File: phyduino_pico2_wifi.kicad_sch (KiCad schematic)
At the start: 94 parts, among them J6 GT-USB-7047A, J9 GT-USB-7047A, Q1 SP30P25NQ, Q2 SP30P25NQ, U10 AP63200WU, U108 TPS2121RUXR, U109 TPS2121RUXR, U11 ESP32-C6-MINI-1-H4, U110 TPS2121RUXR, U6 AP33772SDKZ-13-FA02, U8 AP63200WU, U9 TPUSBLC6-2P6

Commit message: Built board without USB-PD variant. Not yet complete.
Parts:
- removed C132: 0.1µF, Capacitor_SMD [KL]:C_0402_1005Metric, symbol Device:C_Small
- removed C28: 0.1µF, Capacitor_SMD [KL]:C_1206_3216Metric_Pad1.33x1.80mm_HandSolder, symbol Component - Device [KL]:C_Small
- removed C29, C32: 10μF, Capacitor_SMD [KL]:C_0805_2012Metric_Pad1.18x1.45mm_HandSolder, symbol Component - Device [KL]:C_Small
- removed C30: 1µF, Capacitor_SMD [KL]:C_0402_1005Metric, symbol Component - Device [KL]:C_Small
- removed C31, C6: 0.1µF, Capacitor_SMD [KL]:C_0402_1005Metric, symbol Component - Device [KL]:C_Small
- removed C33, C35: 0.1μF, Capacitor_SMD [KL]:C_0805_2012Metric_Pad1.18x1.45mm_HandSolder, symbol Component - Device [KL]:C_Small
- removed J9: GT-USB-7047A, Connector - PC SMT [UL]:GCT-USBC-GCT_USB4110, symbol KL - Connector:USB_C_Receptacle_USB2.0_16P
- removed Q1, Q2: SP30P25NQ, Package_DFN_QFN [KL]:Diodes_UDFN2020-6_Type-F, symbol UL - Transistors - MOSFET:PMPB27EP
- removed R10: 5mΩ, Resistor_SMD [KL]:R_0603_1608Metric, symbol Component - Device [KL]:R_Small
- removed R11, R12, R7, R8: 5.1kΩ, Resistor_SMD [KL]:R_0402_1005Metric, symbol Component - Device [KL]:R_Small
- removed R143: 35.7kΩ, Resistor_SMD [KL]:R_0402_1005Metric, symbol Device:R_Small
- removed R149: 383kΩ, Resistor_SMD [KL]:R_0402_1005Metric, symbol Device:R_Small
- removed R150: 95.3kΩ, Resistor_SMD [KL]:R_0402_1005Metric, symbol Device:R_Small
- removed R151: 24.3kΩ, Resistor_SMD [KL]:R_0402_1005Metric, symbol Device:R_Small
- removed R37: 5.1kΩ, Resistor_SMD [KL]:R_0402_1005Metric, symbol phyduino_pico:R_Small
- removed R40, R41: 100Ω, Resistor_SMD [KL]:R_0402_1005Metric, symbol phyduino_pico:R_Small
- removed R9: 220kΩ, Resistor_SMD [KL]:R_0805_2012Metric_Pad1.20x1.40mm_HandSolder, symbol Component - Device [KL]:R_Small
- removed TH1: 10kΩ@25°C, Resistor_SMD [KL]:R_0402_1005Metric, symbol Component - Device [KL]:Thermistor_NTC
- removed TP10, TP11, TP13, TP18, TP2, TP4, TP5, TP6, TP7: TestPoint_Small, Component - Test point SMT [UL]:TestPoint_SameSky_CPG-47-TH-B, symbol Connector [KL]:TestPoint_Small
- removed U109: TPS2121RUXR, Package - QFN [UL]:VQFN-HR-12, symbol PMIC - TI:TPS2121RUX
- removed U6: AP33772SDKZ-13-FA02, Package_DFN_QFN [KL]:QFN-24-1EP_4x4mm_P0.5mm_EP2.75x2.75mm, symbol Interface - USB:AP33772S
- removed Z3: ESDA25P35-1U1M-ES, Diode_SMD [KL]:ST_QFN-2L_1.6x1.0mm, symbol phyduino_pico:D_Zener_Filled
- added TP27: TestPoint_Small, Component - Test point SMT [UL]:TestPoint_SameSky_CPG-47-TH-B, symbol Connector [KL]:TestPoint_Small
- C13, C131, C134: footprint Capacitor_SMD [KL]:C_0402_1005Metric -> Capacitor_SMD:C_0402_1005Metric
- C16, C24: value 0.1μF -> 0.1µF; footprint Capacitor_SMD [KL]:C_0805_2012Metric_Pad1.18x1.45mm_HandSolder -> Capacitor_SMD:C_0805_2012Metric_Pad1.18x1.45mm_HandSolder
- C17, C18, C25, C27, C36: footprint Capacitor_SMD [KL]:C_0805_2012Metric_Pad1.18x1.45mm_HandSolder -> Capacitor_SMD:C_0805_2012Metric_Pad1.18x1.45mm_HandSolder
- C19, C23, C37: value 10μF -> 10µF; footprint Capacitor_SMD [KL]:C_0805_2012Metric_Pad1.18x1.45mm_HandSolder -> Capacitor_SMD:C_0805_2012Metric_Pad1.18x1.45mm_HandSolder
- C5, C7: footprint Capacitor_SMD [KL]:C_0805_2012Metric_Pad1.18x1.45mm_HandSolder -> Capacitor_SMD:C_0402_1005Metric
- C9: footprint Capacitor_SMD [KL]:C_1206_3216Metric_Pad1.33x1.80mm_HandSolder -> Capacitor_SMD:C_1206_3216Metric_Pad1.33x1.80mm_HandSolder
- R134: value 42.2kΩ -> 42.2kΩ; footprint Resistor_SMD [KL]:R_0402_1005Metric -> Resistor_SMD:R_0402_1005Metric
- R135, R138: value 21kΩ -> 21kΩ; footprint Resistor_SMD [KL]:R_0402_1005Metric -> Resistor_SMD:R_0402_1005Metric
- R136, R137, R47, R48: value 5.1kΩ -> 5.1kΩ; footprint Resistor_SMD [KL]:R_0402_1005Metric -> Resistor_SMD:R_0402_1005Metric
- R140: value 113kΩ -> 113kΩ; footprint Resistor_SMD [KL]:R_0402_1005Metric -> Resistor_SMD:R_0402_1005Metric
- R141: value 432kΩ -> 432kΩ; footprint Resistor_SMD [KL]:R_0402_1005Metric -> Resistor_SMD:R_0402_1005Metric
- R142: value 52.3kΩ -> 52.3kΩ; footprint Resistor_SMD [KL]:R_0402_1005Metric -> Resistor_SMD:R_0402_1005Metric
- R144, R145: value 24.3kΩ -> 24.3kΩ; footprint Resistor_SMD [KL]:R_0402_1005Metric -> Resistor_SMD:R_0402_1005Metric
- R152: value 35.7kΩ -> 35.7kΩ; footprint Resistor_SMD [KL]:R_0402_1005Metric -> Resistor_SMD:R_0402_1005Metric
- R153: value 10kΩ -> 10kΩ; footprint Resistor_SMD [KL]:R_0402_1005Metric -> Resistor_SMD:R_0402_1005Metric
- R44, R45, R50, R55: footprint Resistor_SMD [KL]:R_0402_1005Metric -> Resistor_SMD:R_0402_1005Metric
- R51: value 47kΩ -> 47kΩ; footprint Resistor_SMD [KL]:R_0805_2012Metric_Pad1.20x1.40mm_HandSolder -> Resistor_SMD:R_0805_2012Metric_Pad1.20x1.40mm_HandSolder
- R52: value 16.5kΩ -> 16.5kΩ; footprint Resistor_SMD [KL]:R_0805_2012Metric_Pad1.20x1.40mm_HandSolder -> Resistor_SMD:R_0805_2012Metric_Pad1.20x1.40mm_HandSolder
- R56: value 196kΩ -> 196kΩ; footprint Resistor_SMD [KL]:R_0805_2012Metric_Pad1.20x1.40mm_HandSolder -> Resistor_SMD:R_0402_1005Metric
- R57: value 62kΩ -> 62kΩ; footprint Resistor_SMD [KL]:R_0805_2012Metric_Pad1.20x1.40mm_HandSolder -> Resistor_SMD:R_0402_1005Metric
- R58: value 157kΩ -> 157kΩ; footprint Resistor_SMD [KL]:R_0805_2012Metric_Pad1.20x1.40mm_HandSolder -> Resistor_SMD:R_0402_1005Metric
- R59: value 30kΩ -> 30kΩ; footprint Resistor_SMD [KL]:R_0805_2012Metric_Pad1.20x1.40mm_HandSolder -> Resistor_SMD:R_0402_1005Metric
- R6: footprint Resistor_SMD [KL]:R_0805_2012Metric_Pad1.20x1.40mm_HandSolder -> Resistor_SMD:R_0805_2012Metric_Pad1.20x1.40mm_HandSolder
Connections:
- net +VUSB_IN is gone; now on net +VIN: U110.7 (IN1)
- net DCDC_5V0_EN: now also TP27.1
- net GND: no longer U110.5 (OV1), U110.6 (PR1)
- net USB_COM_SHIELD: now also J6.S2 (SH); no longer J6.S1 (SH)
- net USB_PMUX1_CP2: now also U110.6 (PR1)
- net USB_PMUX1_OV2: now also U110.5 (OV1)
- no-connect marks 28 -> 17
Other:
- note removed: "5V to 20V"
- note removed: "9V to 20V"
- note removed: ">1.06V"
- note removed: "I^{2}C Addr = 0x52"
- note removed: "Overvoltage Protection = +22.0V"
- moved on the sheet: C131, C134, C16, C17, C18, C19, C23, C24, C25, C27, C36, C5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

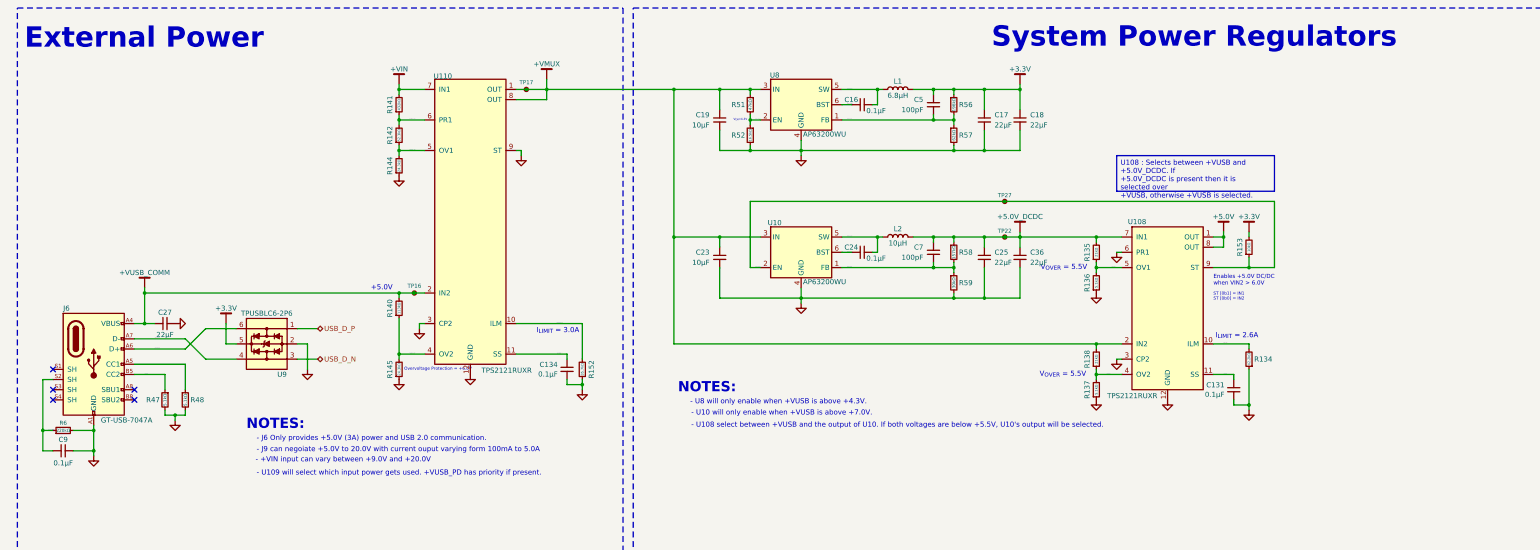
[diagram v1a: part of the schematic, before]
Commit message: Development update : Changed the power input and tree, removed led for communication status.
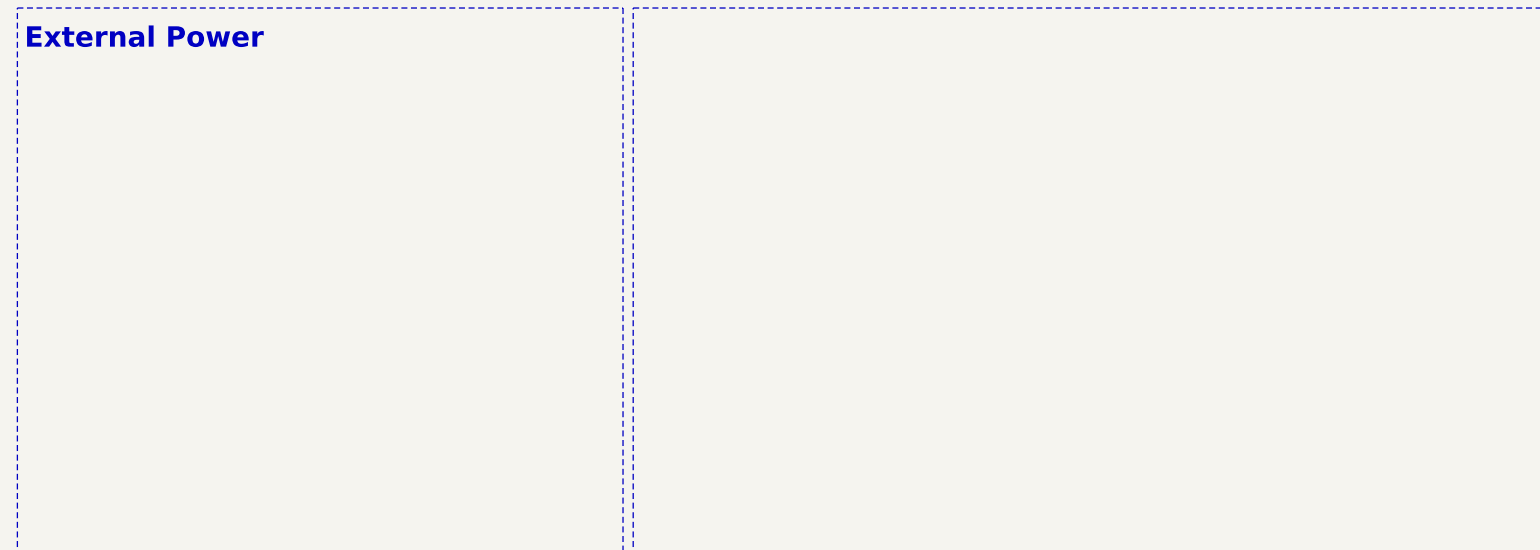
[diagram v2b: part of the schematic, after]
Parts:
- removed C131, C134: 0.1µF, Capacitor_SMD:C_0402_1005Metric, symbol Device:C_Small
- removed C16, C24: 0.1µF, Capacitor_SMD:C_0805_2012Metric_Pad1.18x1.45mm_HandSolder, symbol Component - Device [KL]:C_Small
- removed C17, C18, C25, C27, C36: 22µF, Capacitor_SMD:C_0805_2012Metric_Pad1.18x1.45mm_HandSolder, symbol Component - Device [KL]:C_Small
- removed C19, C23: 10µF, Capacitor_SMD:C_0805_2012Metric_Pad1.18x1.45mm_HandSolder, symbol Component - Device [KL]:C_Small
- removed C5, C7: 100pF, Capacitor_SMD:C_0402_1005Metric, symbol Component - Device [KL]:C_Small
- removed C9: 0.1µF, Capacitor_SMD:C_1206_3216Metric_Pad1.33x1.80mm_HandSolder, symbol Component - Device [KL]:C_Small
- removed J6: GT-USB-7047A, Connector - PC SMT [UL]:GCT-USBC-GCT_USB4110, symbol KL - Connector:USB_C_Receptacle_USB2.0_16P
- removed L1: 6.8µH, Component - Inductor SMT [UL]:L_Bourns_SRP4021HMCT, symbol Inductor - Bourns:L_Bourns_SRP4021HMCT-3R3M
- removed L2: 10µH, Component - Inductor SMT [UL]:L_Bourns_SRP4021HMCT, symbol Inductor - Bourns:L_Bourns_SRP4021HMCT-4R7M
- removed R134: 42.2kΩ, Resistor_SMD:R_0402_1005Metric, symbol Device:R_Small
- removed R135, R138: 21kΩ, Resistor_SMD:R_0402_1005Metric, symbol Device:R_Small
- removed R136, R137: 5.1kΩ, Resistor_SMD:R_0402_1005Metric, symbol Device:R_Small
- removed R140: 113kΩ, Resistor_SMD:R_0402_1005Metric, symbol Device:R_Small
- removed R141: 432kΩ, Resistor_SMD:R_0402_1005Metric, symbol Device:R_Small
- removed R142: 52.3kΩ, Resistor_SMD:R_0402_1005Metric, symbol Device:R_Small
- removed R144, R145: 24.3kΩ, Resistor_SMD:R_0402_1005Metric, symbol Device:R_Small
- removed R152: 35.7kΩ, Resistor_SMD:R_0402_1005Metric, symbol Device:R_Small
- removed R153: 10kΩ, Resistor_SMD:R_0402_1005Metric, symbol Device:R_Small
- removed R47, R48: 5.1kΩ, Resistor_SMD:R_0402_1005Metric, symbol phyduino_pico:R_Small
- removed R51: 47kΩ, Resistor_SMD:R_0805_2012Metric_Pad1.20x1.40mm_HandSolder, symbol phyduino_pico:R_Small
- removed R52: 16.5kΩ, Resistor_SMD:R_0805_2012Metric_Pad1.20x1.40mm_HandSolder, symbol phyduino_pico:R_Small
- removed R56: 196kΩ, Resistor_SMD:R_0402_1005Metric, symbol phyduino_pico:R_Small
- removed R57: 62kΩ, Resistor_SMD:R_0402_1005Metric, symbol phyduino_pico:R_Small
- removed R58: 157kΩ, Resistor_SMD:R_0402_1005Metric, symbol phyduino_pico:R_Small
- removed R59: 30kΩ, Resistor_SMD:R_0402_1005Metric, symbol phyduino_pico:R_Small
- removed R6: 220kΩ, Resistor_SMD:R_0805_2012Metric_Pad1.20x1.40mm_HandSolder, symbol Component - Device [KL]:R_Small
- removed TP16, TP17, TP22, TP27: TestPoint_Small, Component - Test point SMT [UL]:TestPoint_SameSky_CPG-47-TH-B, symbol Connector [KL]:TestPoint_Small
- removed U10, U8: AP63200WU, Package_TO_SOT_SMD [KL]:TSOT-23-6_HandSoldering, symbol Power - Switching Regulator [KL]:AP63200WU
- removed U108, U110: TPS2121RUXR, Package - QFN [UL]:VQFN-HR-12, symbol PMIC - TI:TPS2121RUX
- removed U9: TPUSBLC6-2P6, Package_TO_SOT_SMD [KL]:SOT-666, symbol Protection - Signal:USBLC6-2P6
- C37: Variant ADV_SMT -> STUDENT
- TP14, TP8, TP9: Variant (none) -> IGNORE
- U11: Variant (none) -> ADV_SMT
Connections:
- no-connect marks 17 -> 12
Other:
- note removed: "+5.0V"
- note removed: "- +VIN input can vary between +9.0V and +20.0V"
- note removed: "- J6 Only provides +5.0V (3A) power and USB 2.0 communication."
- note removed: "- J9 can negoiate +5.0V to 20.0V with current ouput varying form 100mA to 5.0A"
- note removed: "- U10 will only enable when +VUSB is above +7.0V."
- note removed: "- U108 select between +VUSB and the output of U10. If both voltages are below +5.5V, U10's output will be selected."
- note removed: "- U109 will select which input power gets used. +VUSB_PD has priority if present."
- note removed: "- U8 will only enable when +VUSB is above +4.3V."
- note removed: "Enables +5.0V DC/DC when VIN2 > 6.0V"
- note removed: "I_{LIMIT} = 2.6A"
- note removed: "I_{LIMIT} = 3.0A"
- note removed: "Overvoltage Protection = +6.0V"
- note removed: "ST [0b1] = IN1 ST [0b0] = IN2"
- note removed: "System Power Regulators"
- note removed: "V_{EN}=4.3V"
- note removed: "V_{OVER} = 5.5V"

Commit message: Development update : Initial design review changes and PCB routing.
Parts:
- R44, R45: value 1.1kΩ -> 10kΩ
- R50, R55: DIGIKEY PN 13-RC0402FR-131K1LCT-ND -> (none); DIGKEY MANUFACTURER YAGEO -> (none); LCSC MANUFACTURER FOJAN -> (none); LCSC PN C2909306 -> (none); PN FRC0402F1101TS -> (none)
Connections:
- net +3.3V: now also R44.1
- net GND: no longer R44.2
- net WIFI_BOOT1: now also R44.2; no longer R44.1
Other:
- note added: "NOTE: Set ENA pin to 'L' before changing BOOT1 pin. Once changed set ENA to 'H' to boot WiFi module."
- note removed: "External Power"
- note removed: "Set boot mode to Download Boot (IO8 = 0b1, IO9 = 0b0)"
- note removed: "UART/USB Firmware download"
- moved on the sheet: C13, C37, R44, R45, R50, R55, TP14, TP8, TP9, U11
